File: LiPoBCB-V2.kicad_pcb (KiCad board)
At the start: 2 copper layers, 30.1 x 16.4 mm, 27 parts, among them J1 USB-C_6_pin_receptacle, J2 Conn_01x02, Q1 Q_Dual_PMOS_S1G1D2S2G2D1, U1 ETA9740

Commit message: added polygons
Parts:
- moved J2 1.02 mm to (169.9, 97.8)
- moved C2 0.57 mm to (162.6, 97.7)
- moved R1 0.57 mm to (164.1, 97.7)
- moved R4 0.57 mm to (167.1, 97.7)
- moved R5 0.57 mm to (165.6, 97.7)
- moved C1 0.38 mm to (163.8, 93.1)
- moved C3 0.38 mm to (165.6, 92.9)
- moved C4 0.24 mm to (161.8, 91.5)
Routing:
- net GND: track 49.8 -> 1.24 mm, vias 0 -> 6
- net /CC2: track 0.00 -> 17.6 mm, vias 0 -> 2
- net /CC1: track 0.00 -> 17.3 mm, vias 0 -> 2
- net /BAT: track 16.9 -> 0.35 mm, vias 2 -> 7
- net +5V: track 10.7 -> 0.91 mm
- net /VBUS: track 6.38 -> 0.36 mm, vias 0 -> 4
- net /ISET: track 0.00 -> 5.77 mm, vias 0 -> 2
- net /SW: track 3.61 -> 0.00 mm
- net /SW_GATE: track 14.9 -> 13.9 mm
- net Net-(C6-Pad2): track 15.1 -> 16.0 mm
- added copper zone on F.Cu, net +5V
- added copper zone on B.Cu, net /BAT
- added copper zone on F.Cu, net /BAT
- added copper zone on F.Cu, net /SW
- added copper zone on B.Cu, net /VBUS
- added copper zone on F.Cu, net /VBUS
- added copper zone on B.Cu, net GND
- added copper zone on F.Cu, net GND

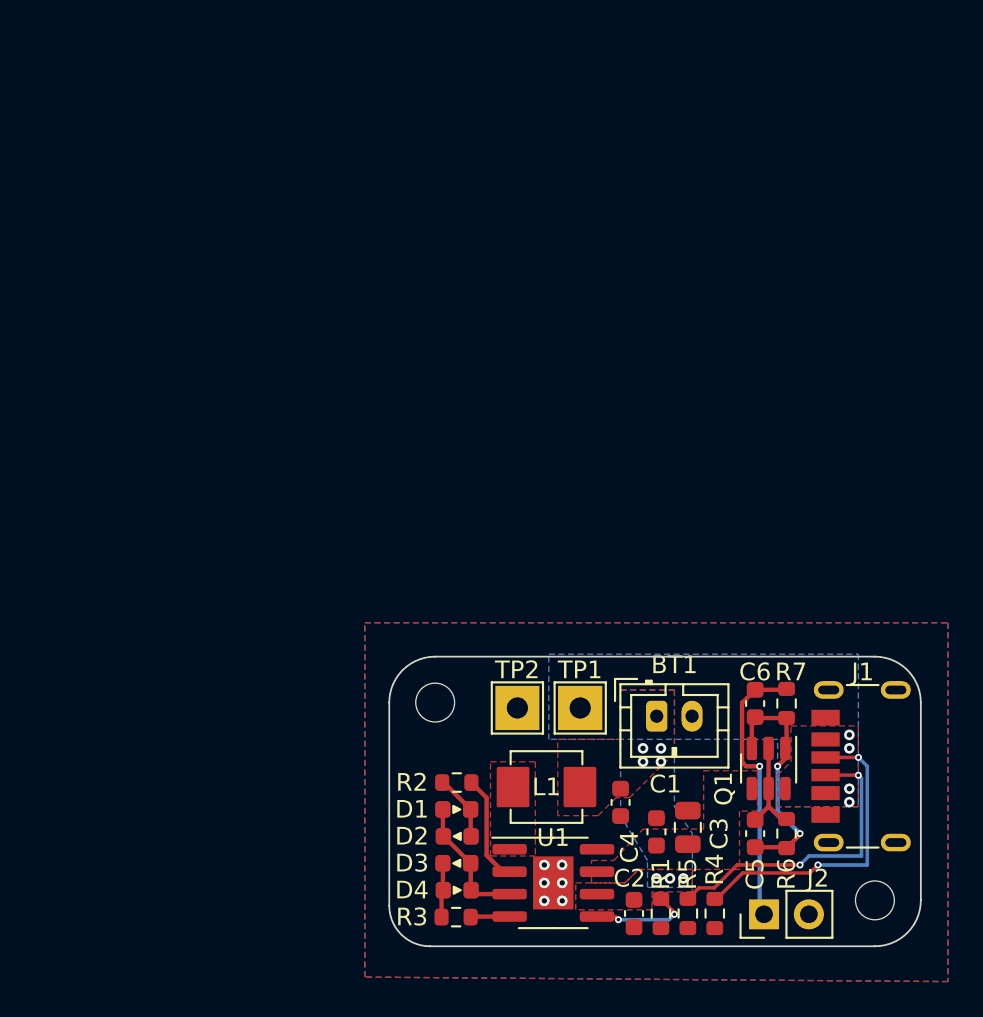
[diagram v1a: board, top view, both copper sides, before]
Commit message: moved pcb, redefined edge
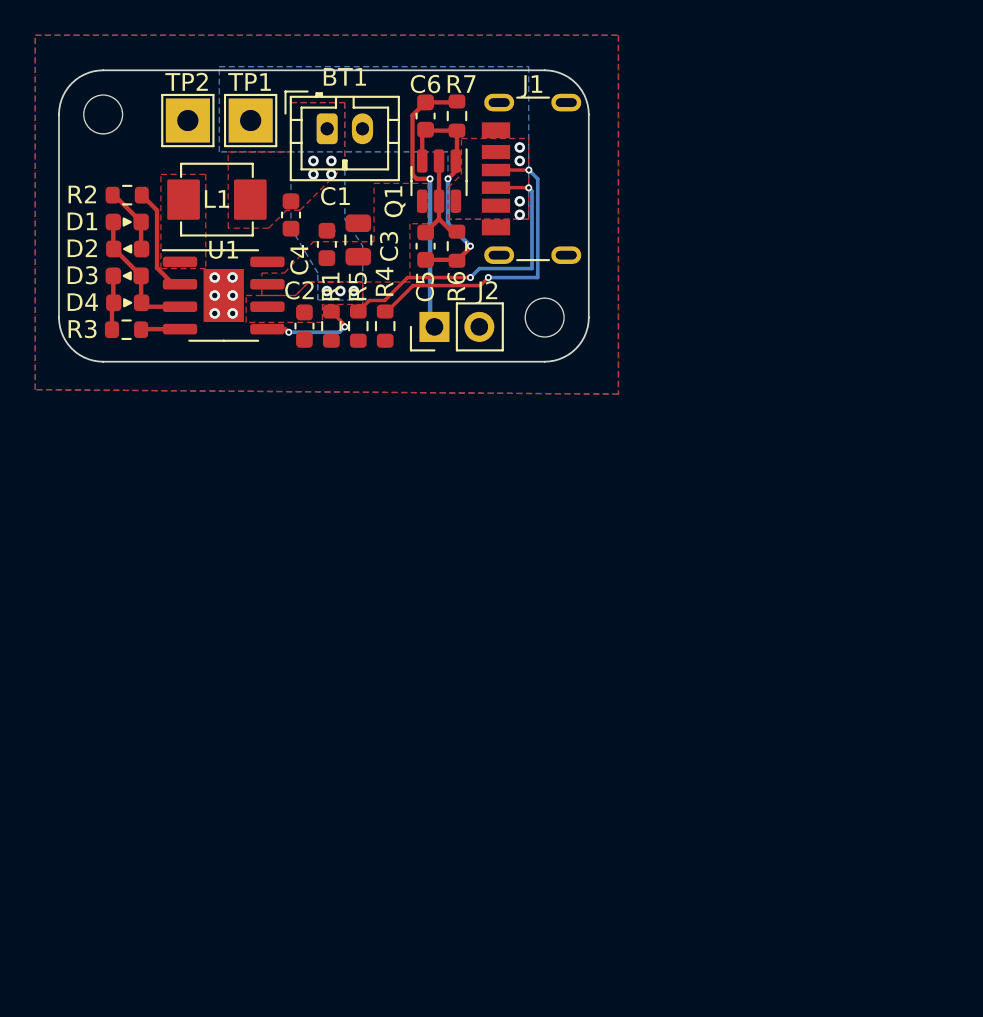
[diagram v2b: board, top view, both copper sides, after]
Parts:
- moved H2 38.2 mm to (132.5, 52.5)
- moved C1 38.1 mm to (145.2, 59.9)
- moved C5 38.1 mm to (150.8, 60.0)
- moved C6 38.1 mm to (150.8, 52.6)
- moved D3 38.1 mm to (133.9, 61.6)
- moved J1 38.1 mm to (154.7, 56.1)
- moved Q1 38.1 mm to (151.5, 56.3)
- moved C4 38.1 mm to (143.1, 58.2)
- moved D1 38.1 mm to (133.9, 58.6)
- moved R2 38.1 mm to (133.9, 57.1)
- moved R6 38.1 mm to (152.5, 60.0)
- moved R7 38.1 mm to (152.5, 52.6)
- moved BT1 38.1 mm to (145.2, 53.3)
- moved C2 38.1 mm to (143.9, 64.5)
- moved C3 38.1 mm to (146.9, 59.6)
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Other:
- board size 30.1 x 16.4 mm -> 30 x 16.5 mm
